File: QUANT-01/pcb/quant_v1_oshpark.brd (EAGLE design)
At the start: 127.6 x 81.3 mm, 77 parts, among them SW1 SUBMINI_SPDT, SW2 SUBMINI_SPDT, SW3 SUBMINI_SPDT, SW4 SUBMINI_SPDT, SW5_MODE SUBMINI_SPDT, U3 MCP6002, U4 TL074_

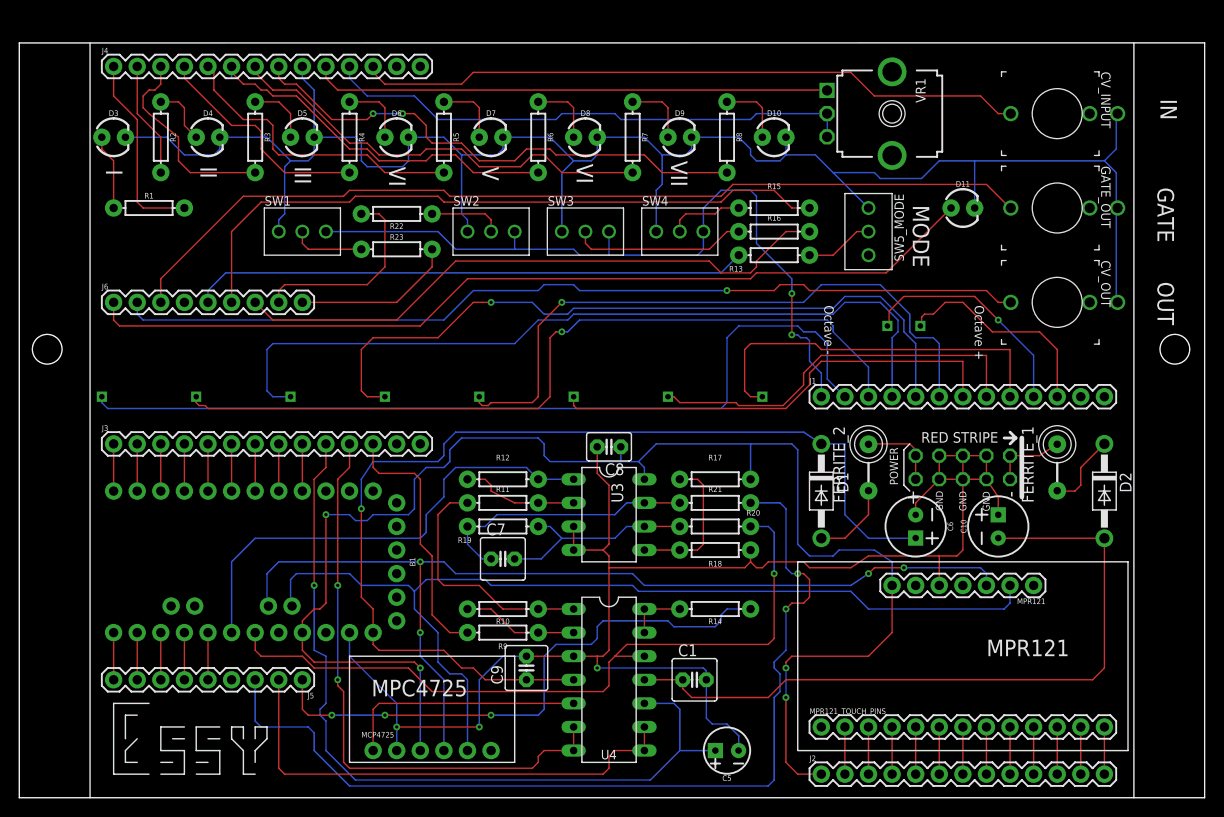
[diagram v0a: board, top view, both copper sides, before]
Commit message: completed first PCB run with OSH park.  Beginning to make mods to add octaves.
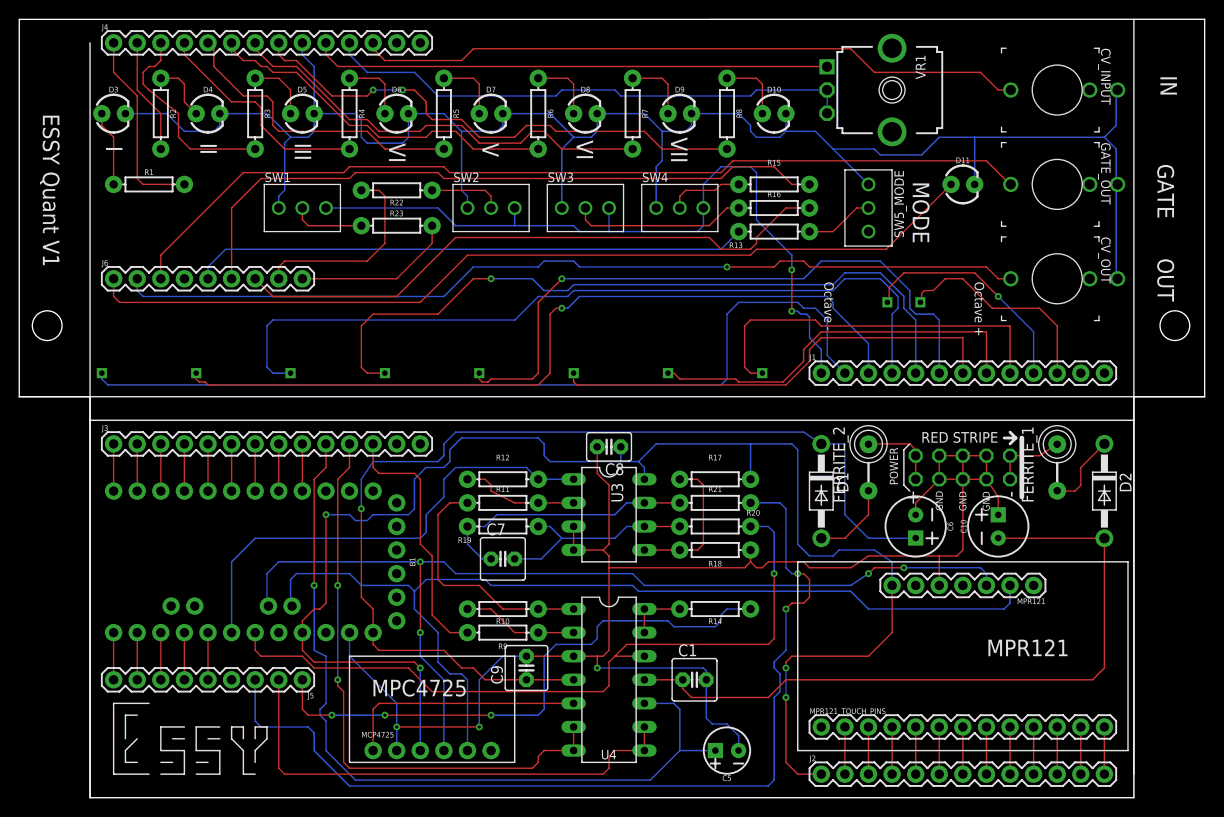
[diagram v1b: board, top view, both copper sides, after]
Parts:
- moved CV_INPUT 2.54 mm to (111.8, 76.2)
- moved D11 2.54 mm to (101.6, 66.0)
- moved GATE_OUT 2.54 mm to (111.8, 66.0)
- moved J4 2.54 mm to (10.2, 81.3)
- moved R1 2.54 mm to (14.0, 66.0)
- moved R15 2.54 mm to (81.3, 66.0)
- moved U$1 2.54 mm to (99.1, 53.3)
- moved U$2 2.54 mm to (91.4, 53.3)
- moved VR1 2.54 mm to (94.0, 76.2)
- moved CV_OUT 2.54 mm to (111.8, 55.9)
- moved J1 2.54 mm to (86.4, 45.7)
- moved J6 2.54 mm to (10.2, 55.9)
- moved R13 2.54 mm to (81.3, 61.0)
- moved R16 2.54 mm to (81.3, 63.5)
- moved R22 2.54 mm to (40.6, 65.4)
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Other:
- board size 127.6 x 81.3 mm -> 127.6 x 83.8 mm
- board text added: "ESSY Quant V1"
